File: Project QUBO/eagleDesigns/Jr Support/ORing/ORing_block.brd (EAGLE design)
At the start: 96.5 x 101.6 mm, 83 parts

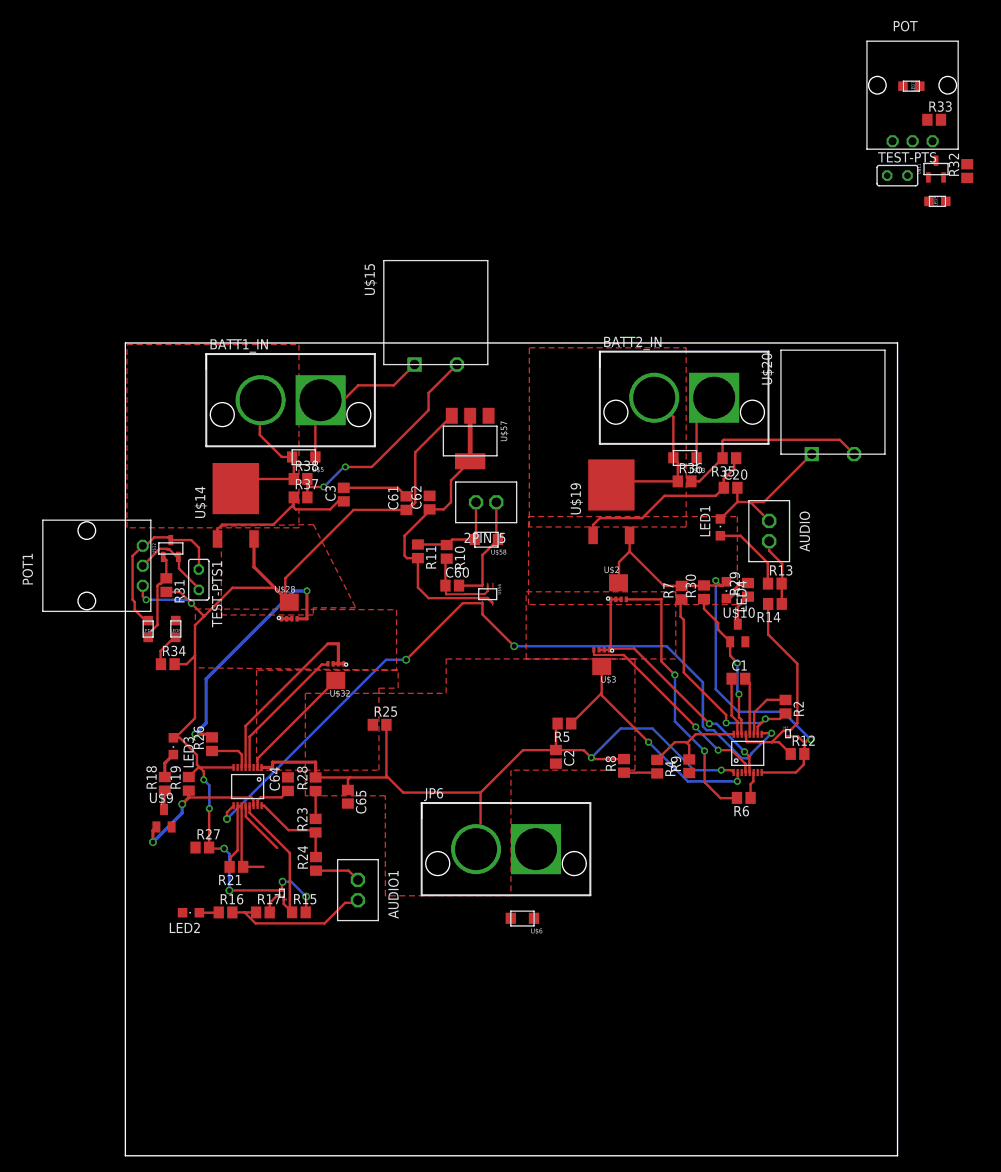
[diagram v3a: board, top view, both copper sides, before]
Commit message: 
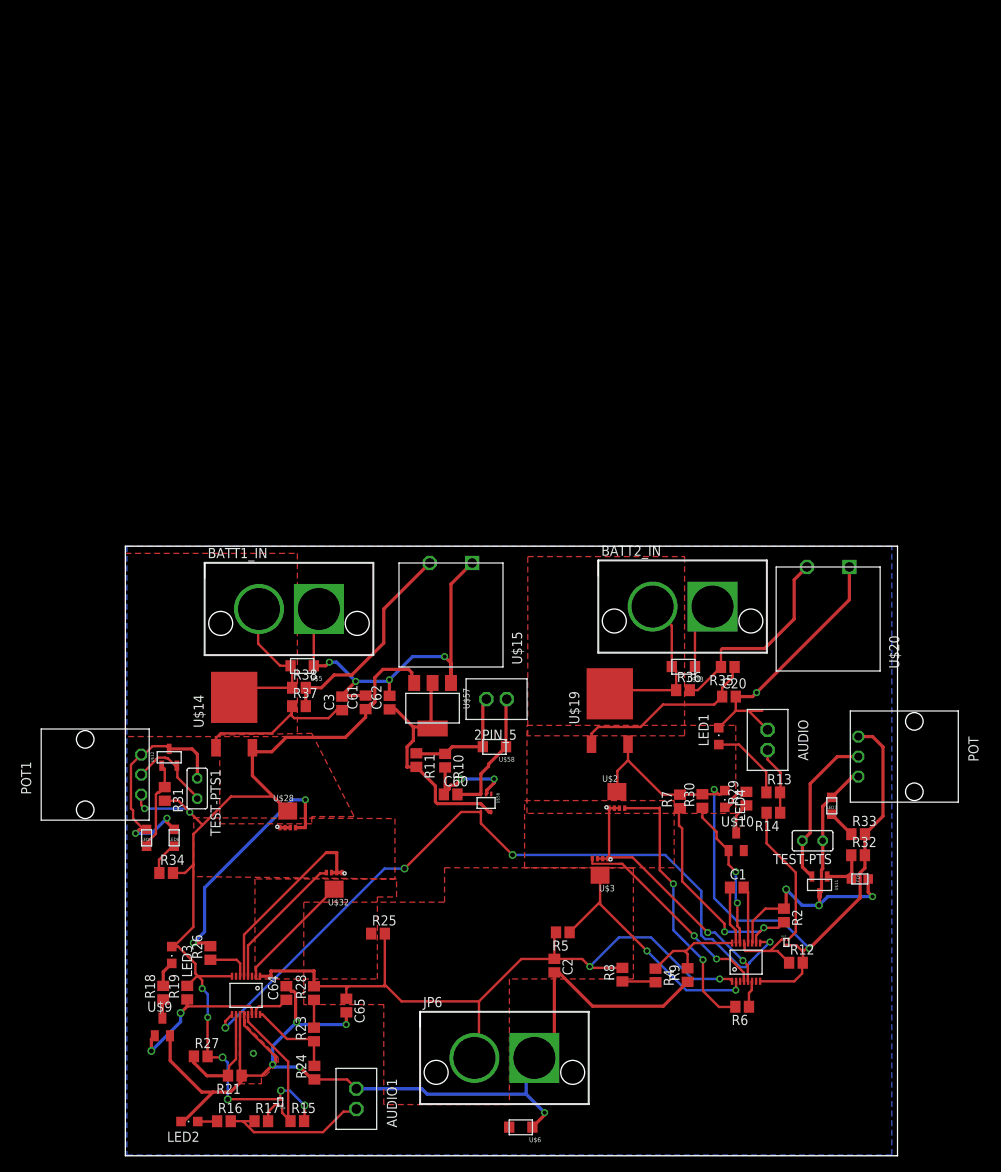
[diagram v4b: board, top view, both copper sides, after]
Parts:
- moved U$11 90.7 mm to (86.8, 33.9), turned to 270 degrees
- moved LED7 90.5 mm to (88.3, 43.8), turned to 90 degrees
- moved R33 89.8 mm to (91.6, 40.2)
- moved R32 86.6 mm to (91.6, 37.6), turned to 0 degrees
- moved LED5 85.3 mm to (91.8, 34.6)
- moved TEST-PTS 83.8 mm to (85.9, 39.4), turned to 180 degrees
- moved POT 77.2 mm to (91.6, 49.9), turned to 270 degrees
- moved U$57 33.7 mm to (38.4, 56.0)
- moved BATT1_IN 26.1 mm to (20.4, 68.3)
- moved C3 26.1 mm to (27.1, 56.5)
- moved TEST-PTS1 26.1 mm to (8.98, 45.9)
- moved U$14 26.1 mm to (13.6, 57.3)
- moved AUDIO 26.1 mm to (80.3, 52.0)
- moved AUDIO1 26.1 mm to (28.9, 7.11)
- moved C1 26.1 mm to (76.4, 33.5)
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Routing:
- net GND: track 116.9 -> 313.2 mm, vias 0 -> 16
- net V_BATT2: track 61.6 -> 94.0 mm
- net N$23: track 0.00 -> 19.9 mm
- net V_BATT1: track 134.9 -> 127.2 mm
- net N$13: track 37.6 -> 31.3 mm
- net N$30: track 0.00 -> 5.99 mm
- net N$39: track 8.08 -> 13.8 mm
- net N$33: track 0.00 -> 3.51 mm
- net N$12: track 12.1 -> 14.8 mm
- net N$49: track 10.7 -> 13.0 mm, vias 0 -> 2
- net N$48: track 14.2 -> 16.1 mm
- net N$41: track 28.6 -> 26.8 mm, vias 2 -> 0
- net N$36: track 24.5 -> 25.2 mm
- added copper zone on layer 1, net GND
- added copper zone on layer 16, net GND
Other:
- board size 96.5 x 101.6 mm -> 96.5 x 76.2 mm

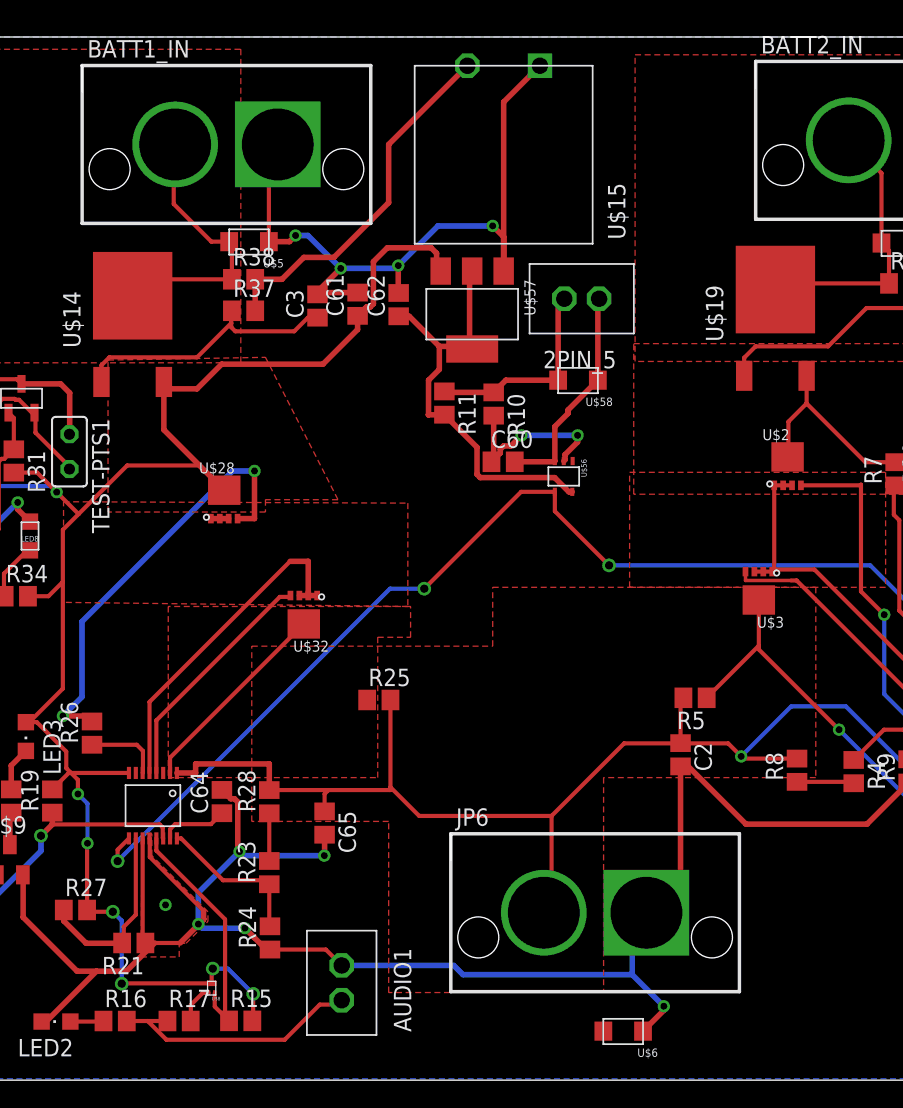
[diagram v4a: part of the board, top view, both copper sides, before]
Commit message: 
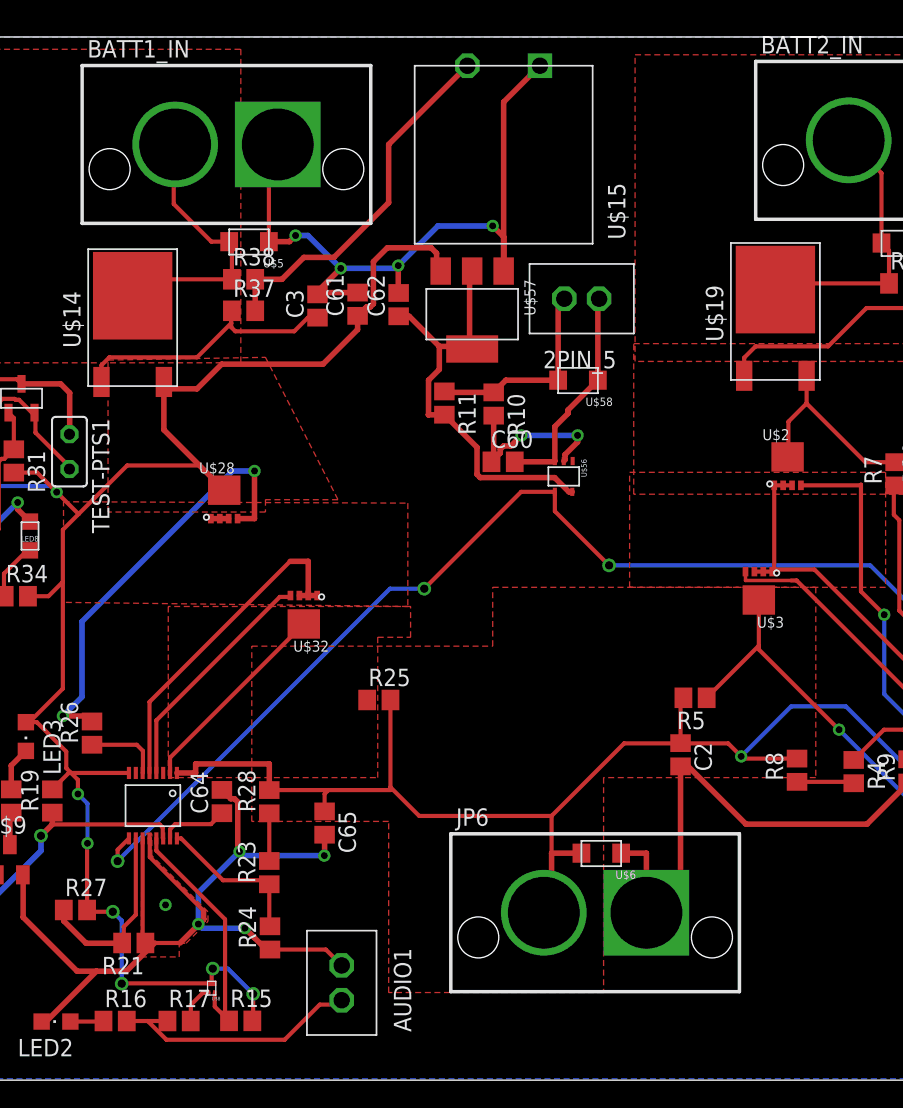
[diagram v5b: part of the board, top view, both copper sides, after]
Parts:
- moved U$6 13.1 mm to (47.8, 16.6)
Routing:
- net GND: track 313.2 -> 287.2 mm, vias 16 -> 15
- net V_BATT: track 92.0 -> 95.5 mm
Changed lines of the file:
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@@
 <element name="R32" library="resistor" package="R0805" value="330" x="91.59" y="37.57"/>
 <element name="R4" library="resistor" package="R0805" value="51k" x="66.27" y="22.54" rot="R270"/>
-<element name="R5" library="resistor" package="R0805" value="5m" x="54.68" y="27.93" rot="R180"/>
+<element name="R5" library="resistor" package="R0805" value="5m" x="54.68" y="27.93" smashed="yes" rot="R180">
+<attribute name="NAME" x="55.442" y="26.914" size="1.27" layer="25" rot="R180"/>
+<attribute name="VALUE" x="55.442" y="30.216" size="1.27" layer="27" rot="R180"/>
+</element>
 <element name="R6" library="resistor" package="R0805" value="10\" x="77.1" y="18.63" rot="R180"/>
 <element name="R7" library="resistor" package="R0805" value="200k" x="69.33" y="44.29" rot="R90"/>
@@
 <element name="U$57" library="ONSemi" package="SOT-223" value="NCP1117" x="38.4" y="55.95" rot="R180"/>
 <element name="U$58" library="diode" package="DO-219AB" value="VTVS" x="46.13" y="51.13" rot="R180"/>
-<element name="U$6" library="diode" package="DO-219AB" value="VTVS" x="49.43" y="3.58" rot="R180"/>
+<element name="U$6" library="diode" package="DO-219AB" value="VTVS" x="47.83" y="16.58" rot="R180"/>
 <element name="U$7" library="transistor-fet" package="AP02002" value="DMP32D5SFB" x="82.63" y="26.67" rot="R270"/>
 <element name="U$8" library="transistor-fet" package="AP02002" value="DMP32D5SFB" x="19.37" y="6.72" rot="R90"/>
@@
 <wire x1="21.8" y1="11.1" x2="18.7" y2="11.1" width="0.4064" layer="16"/>
 <wire x1="18.7" y1="11.1" x2="18.4" y2="11.4" width="0.4064" layer="16"/>
-<wire x1="28.87" y1="8.38" x2="37.04865" y2="8.38" width="0.4064" layer="16"/>
-<wire x1="37.04865" y1="8.38" x2="37.71985" y2="7.7088" width="0.4064" layer="16"/>
-<wire x1="52.4" y1="5.4" x2="50.0912" y2="7.7088" width="0.4064" layer="16"/>
-<wire x1="37.71985" y1="7.7088" x2="50.0912" y2="7.7088" width="0.4064" layer="16"/>
-<via x="52.4" y="5.4" extent="1-16" drill="0.5"/>
-<wire x1="52.4" y1="5.4" x2="52.4" y2="5.1" width="0.4064" layer="1"/>
-<wire x1="52.4" y1="5.1" x2="50.88" y2="3.58" width="0.4064" layer="1"/>
-<wire x1="50.0912" y1="7.7088" x2="50.0912" y2="11.1947" width="0.4064" layer="16"/>
-<wire x1="50.0912" y1="11.1947" x2="51.1265" y2="12.23" width="0.4064" layer="16"/>
 <wire x1="53.62" y1="14.7235" x2="53.62" y2="22.92" width="0.4064" layer="1"/>
-<wire x1="53.62" y1="14.7235" x2="51.1265" y2="12.23" width="0.4064" layer="1"/>
+<wire x1="51.1265" y1="12.23" x2="53.62" y2="14.7235" width="0.4064" layer="1"/>
 <wire x1="53.62" y1="22.92" x2="54.18" y2="22.92" width="0.4064" layer="1"/>
 <wire x1="54.18" y1="22.92" x2="58.4" y2="18.7" width="0.4064" layer="1"/>
@@
 <vertex x="95.8" y="76.2"/>
 </polygon>
+<wire x1="49.28" y1="16.58" x2="51.1265" y2="16.58" width="0.4064" layer="1"/>
+<wire x1="51.1265" y1="16.58" x2="51.1265" y2="12.23" width="0.4064" layer="1"/>
 <wire x1="77.28" y1="33.53" x2="77.28" y2="38.13" width="0" layer="19" extent="1-1"/>
 <wire x1="78.34" y1="26.59" x2="77.84" y2="26.59" width="0" layer="19" extent="1-1"/>
@@
 <wire x1="53.64" y1="24.6" x2="49.5" y2="24.6" width="0.3048" layer="1"/>
 <wire x1="49.5" y1="24.6" x2="44.2" y2="19.3" width="0.3048" layer="1"/>
-<wire x1="44.2" y1="19.3" x2="44.2" y2="12.7965" width="0.3048" layer="1"/>
+<wire x1="44.2" y1="15.24" x2="44.2" y2="19.3" width="0.3048" layer="1"/>
+<wire x1="44.2" y1="15.24" x2="44.2" y2="12.7965" width="0.3048" layer="1"/>
 <wire x1="44.2" y1="12.7965" x2="43.6335" y2="12.23" width="0.3048" layer="1"/>
 <wire x1="44.2" y1="19.3" x2="34.53" y2="19.3" width="0.3048" layer="1"/>
@@
 <wire x1="18.2" y1="23.1" x2="23.58" y2="23.1" width="0.4064" layer="1"/>
 <wire x1="23.58" y1="23.1" x2="23.58" y2="21.19" width="0.4064" layer="1"/>
-<wire x1="43.6335" y1="12.23" x2="47.98" y2="3.58" width="0" layer="19" extent="1-1"/>
+<wire x1="46.38" y1="16.58" x2="44.2" y2="16.58" width="0.4064" layer="1"/>
+<wire x1="44.2" y1="16.58" x2="44.2" y2="15.24" width="0.4064" layer="1"/>
 </signal>
 <signal name="N$39">

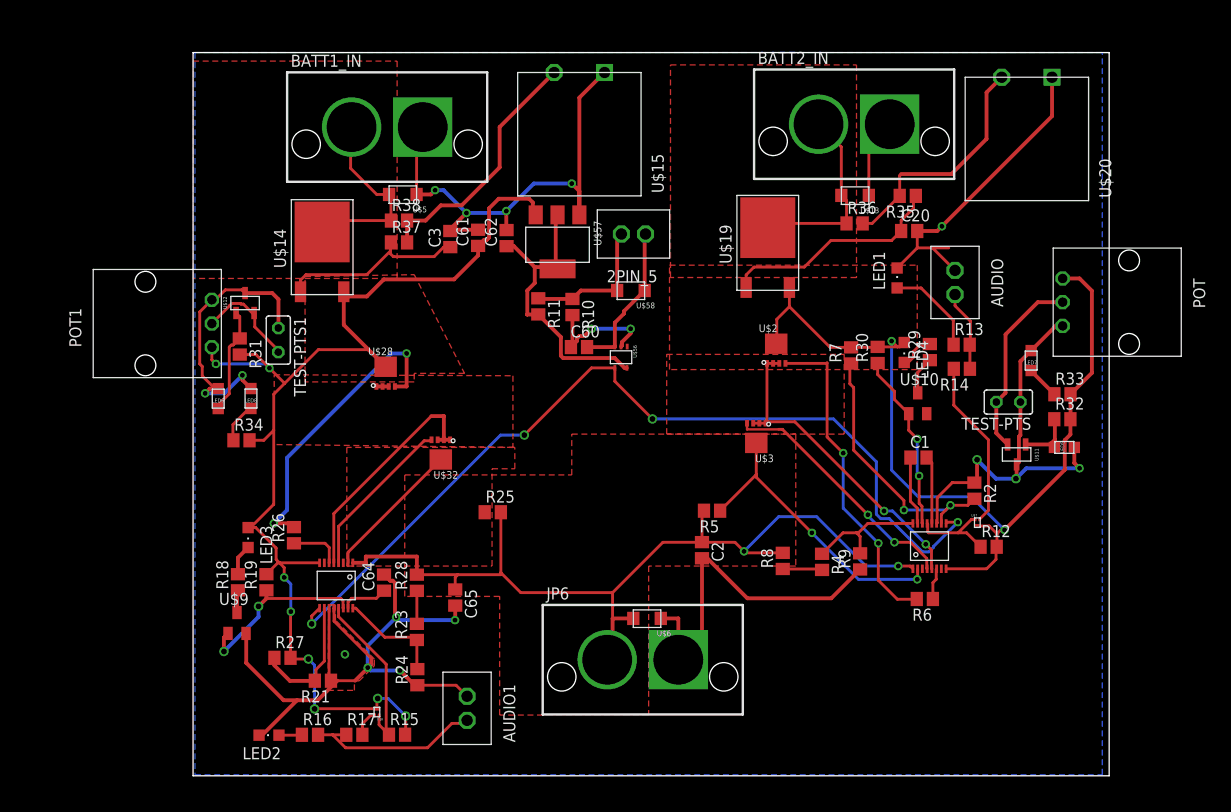
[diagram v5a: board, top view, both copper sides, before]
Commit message: 
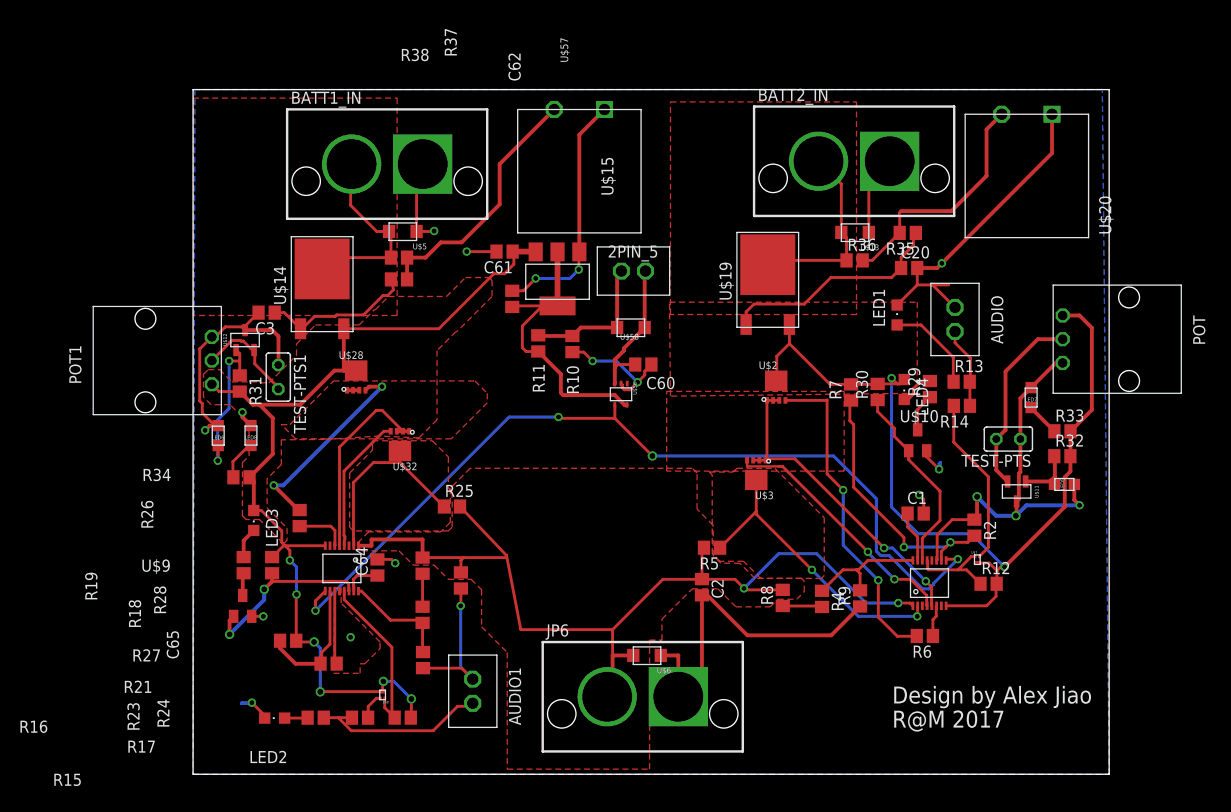
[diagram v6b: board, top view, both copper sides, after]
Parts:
- R15: value (none) -> 20k+
- moved C3 20.8 mm to (7.75, 48.8), turned to 180 degrees
- moved C60 7.03 mm to (47.4, 43.3), turned to 180 degrees
- moved C62 6.43 mm to (33.6, 50.2)
- moved C1 5.91 mm to (76.1, 27.6)
- moved U$32 4.39 mm to (21.8, 34.9)
- moved R25 4.34 mm to (27.3, 28.4)
- moved BATT2_IN 3.90 mm to (69.7, 64.8)
- moved LED1 3.90 mm to (74.2, 48.5)
- moved R14 3.90 mm to (81.0, 39.0)
- moved R30 3.90 mm to (72.1, 40.4)
- moved R33 3.90 mm to (91.6, 36.3)
- moved R36 3.90 mm to (69.7, 54.3)
- moved R37 3.90 mm to (21.7, 52.3)
- moved TEST-PTS 3.90 mm to (85.9, 35.5)
- moved U$12 3.90 mm to (5.48, 45.9)
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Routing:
- net GND: track 287.2 -> 229.3 mm, vias 15 -> 17
- net V_BATT1: track 127.2 -> 102.9 mm, vias 8 -> 6
- net N$59: track 31.6 -> 21.4 mm
- net V_BATT: track 95.5 -> 101.2 mm
- net N$60: track 14.9 -> 20.2 mm
- net N$32: track 11.3 -> 16.6 mm, vias 0 -> 2
- net N$40: track 20.0 -> 16.1 mm
- net N$54: track 26.1 -> 22.2 mm
- net N$61: track 17.4 -> 14.6 mm
- net N$14: track 96.0 -> 93.4 mm
- net N$6: track 7.25 -> 5.38 mm
- net N$28: track 18.9 -> 20.4 mm, vias 2 -> 0
- net N$53: track 4.94 -> 3.97 mm
- net N$13: track 31.3 -> 32.1 mm
- net N$48: track 16.1 -> 15.6 mm
- added copper zone on layer 1, net N$10
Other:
- board size 96.5 x 76.2 mm -> 96.5 x 72.1 mm
- board text added: "Design by Alex Jiao"
- board text added: "R@M 2017"
